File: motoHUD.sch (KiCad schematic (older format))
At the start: 54 parts

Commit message: update
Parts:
- added C? (x2): 10u, symbol Device:C_Small
- added C? (x2): 22u, symbol Device:C_Small
- added C? (x2): 2,2u, symbol Device:C_Small
- added D? (x3): 1N4148, Diode_THT:D_DO-35_SOD27_P7.62mm_Horizontal, symbol Diode:1N4148
- added J?: SIG_CONN, symbol Connector:Conn_01x03_Female
- added J?: Ignition 12V, symbol Connector:Conn_01x02_Female
- added J?: Constant 12V, symbol Connector:Conn_01x02_Female
- added R? (x3): 10k, symbol Device:R
- added R? (x3): 3k3, symbol Device:R
- added R?: 100k, symbol Device:R
- added R?: 22k, symbol Device:R
- added R?: 75R, symbol Device:R
- added TP?: RTCPWR, symbol Connector:TestPoint
- added U?: AZ1117-3.3, symbol Regulator_Linear:AZ1117-3.3
- added U?: AZ1117-5.0, symbol Regulator_Linear:AZ1117-5.0
- added U?: LM311, symbol Comparator:LM311
- added U?: PC817, Package_DIP:DIP-4_W7.62mm, symbol Isolator:PC817
- Q?: value Q_NMOS_DGS -> ????
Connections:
- net +3V3: now also C?.1, U?.2 (VO)
- net +5V: now also C?.1, C?.1, U?.2 (VO), U?.3 (VI)
- net GND: now also U?.23 (VSS), U?.35 (VSS), U?.47 (VSS), U?.8 (VSSA), C?.2, C?.2, C?.2, C?.2, C?.2, C?.2, J?.1 (Pin_1), J?.1 (Pin_1), R?.2, R?.2, R?.2, R?.2, U?.1 (GND), U?.1 (GND)
- net SIG_BLINK: now also R?.1, R?.2
- net SIG_HIBEAM: now also R?.1, R?.2
- net SIG_NEUTRAL: now also R?.1, R?.2
- net +BATT: now reaches U?.1 (VBAT)
- net +BATT: now also C?.1, R?.1, R?.2, TP?.1
- new net: J?.1 (Pin_1), R?.1
- new net: J?.2 (Pin_2), R?.1
- new net: J?.3 (Pin_3), R?.1
- new net: D?.1 (K), R?.1 (x2)
- new net: D?.2 (A), J?.2 (Pin_2) (x2)
- new net: C?.1, R?.2
- new net VCC: C?.1, D?.1 (K), U?.3 (VI)
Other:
- note added: "12-15V\nIgnition"
- note added: "2,9V for 12V in\n3,7V for 15V in\nMCU pins 5V tolerant"
- note added: "3.3V POWER RAIL"
- note added: "5V POWER RAIL"
- note added: "Backlight LED\nUf=3,2V\nIf=60mA"
- note added: "IGNITION INPUT"
- note added: "RC=10s"
- note added: "RTC POWER RAIL"
- note added: "RTC rated 1,8V-3,6V 20-24uA\n\n+BATT at\n2,37V at 12V 21uA load\n3,22V at 16V 26uA load\n134uA current consumption"
- note added: "SIGNAL INPUTS"
- note added: "VBAT 1.8-3,6V"
- note added: "White LED\nUf=3,2V"
- note added: "fc=964Hz"
- moved on the sheet: C?, D?, J?, M?, Q?, R?, TP?, U?, Y?

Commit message: RPM sensing
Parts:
- removed C?: 2,2u, symbol Device:C_Small
- removed D?: 1N4148, Diode_THT:D_DO-35_SOD27_P7.62mm_Horizontal, symbol Diode:1N4148
- removed J?: Conn_01x03_MountingPin, symbol Connector_Generic_MountingPin:Conn_01x03_MountingPin
- removed J?: SIG_CONN, symbol Connector:Conn_01x03_Female
- removed R?: 100k, symbol Device:R
- removed R?: 75R, symbol Device:R
- removed U?: PC817, Package_DIP:DIP-4_W7.62mm, symbol Isolator:PC817
- added C14, C15, C16: 0,1u, symbol Device:C_Small
- added C9: 2,2u, symbol Device:C_Small
- added F1: C1F-375, symbol Device:Fuse_Small
- added J6: SIG_RPM, symbol Connector:Conn_01x02_Female
- added J7: Conn_01x04_Female, symbol Connector:Conn_01x04_Female
- added J9: Conn_01x03_Male, symbol Connector:Conn_01x03_Male
- added R9: 10K, symbol Device:R
- gave numbers to parts that had none: 73
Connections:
- net +3V3: now also U3.8 (V+), C14.1, C15.1, C16.1, C9.1, R9.2
- net GND: now also U3.1 (GND), U3.3 (-), U3.4 (V-), C14.2, C15.2, C16.2, C9.2, J6.1 (Pin_1), J7.1 (Pin_1), J9.1 (Pin_1)
- net SIG_RPM: now also U3.7, R9.1
- net SWDCLK: now also J9.3 (Pin_3)
- net SWDIO: now also J9.2 (Pin_2)
- net at R16.1: now also J7.2 (Pin_2)
- net at R19.1: now also J7.3 (Pin_3)
- net at R21.1: now also J7.4 (Pin_4)
- net at J2.2 (Pin_2): now also F1.1; no longer D2.2 (A)
- net at U3.2 (+): now also J6.2 (Pin_2)
- net at U3.5 (BAL): now also U3.6 (STRB)
- new net: D2.2 (A), F1.2
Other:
- note added: "High level\n2,9V for 12V in\n3,7V for 15V in\nMCU pins 5V tolerant"
- note added: "RPM SENSING"
- note removed: "2,9V for 12V in\n3,7V for 15V in\nMCU pins 5V tolerant"
- note removed: "fc=964Hz"
- moved on the sheet: C1, C10, C11, C12, C13, C2, C5, C6, C7, D1, D2, D7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

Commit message: Updated PCB layout
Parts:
- removed C9: 2,2u, symbol Device:C_Small
- removed J1: Constant 12V, symbol Connector:Conn_01x02_Female
- removed J2: Ignition 12V, symbol Connector:Conn_01x02_Female
- removed J7: Conn_01x04_Female, symbol Connector:Conn_01x04_Female
- added D8: 1N4148, Diode_THT:D_DO-35_SOD27_P7.62mm_Horizontal, symbol Diode:1N4148
- added J1: POWER, Connector_JST:JST_XH_B03B-XH-A_1x03_P2.50mm_Vertical, symbol Connector:Conn_01x03_Female
- added J2: SIGNAL, Connector_JST:JST_XH_B03B-XH-A_1x03_P2.50mm_Vertical, symbol Connector:Conn_01x03_Female
- added R34, R35: 5,1k, Resistor_SMD:R_0805_2012Metric_Pad1.15x1.40mm_HandSolder, symbol Device:R
- added R36, R37: 100K, Resistor_SMD:R_0805_2012Metric_Pad1.15x1.40mm_HandSolder, symbol Device:R
- added R38: 10k, Resistor_SMD:R_0805_2012Metric_Pad1.15x1.40mm_HandSolder, symbol Device:R
- added R39: 20M, Resistor_SMD:R_0805_2012Metric_Pad1.15x1.40mm_HandSolder, symbol Device:R
- added TP6: PA0, TestPoint:TestPoint_Pad_D2.5mm, symbol Connector:TestPoint
- added TP7: PA1, TestPoint:TestPoint_Pad_D2.5mm, symbol Connector:TestPoint
- C1, C10, C11, C12, C13, C14, C15, C16, C2, C3, C4, C5, C6, C7: footprint (none) -> Capacitor_SMD:C_0805_2012Metric_Pad1.15x1.40mm_HandSolder
- C8: footprint (none) -> Capacitor_THT:CP_Radial_D8.0mm_P3.50mm
- D3, D4, D5, D6: footprint (none) -> LED_SMD:LED_1206_3216Metric
- D7: footprint (none) -> LED_SMD:LED_1206_3216Metric_Pad1.42x1.75mm_HandSolder
- F1: footprint (none) -> Fuse:Fuse_1206_3216Metric_Pad1.42x1.75mm_HandSolder
- J10: footprint (none) -> motoHUD:ILI9341 FFC
- J3, J4, J6: footprint (none) -> Connector_JST:JST_XH_B02B-XH-A_1x02_P2.50mm_Vertical
- J5: footprint (none) -> Connector_JST:JST_XH_B03B-XH-A_1x03_P2.50mm_Vertical
- J8: footprint (none) -> Connector_USB:USB_Mini-B_Lumberg_2486_01_Horizontal
- J9: footprint (none) -> Connector_PinHeader_2.54mm:PinHeader_1x03_P2.54mm_Vertical
- M1: footprint (none) -> motoHUD:X27-168
- Q1: value ????? -> 2N7002KQ-13; footprint (none) -> Package_TO_SOT_SMD:SOT-23
- Q2: value ???? -> 2N7002KQ-13; footprint (none) -> Package_TO_SOT_SMD:SOT-23
- R1, R10, R11, R12, R13, R14, R15, R16, R17, R18, R19, R2, R20, R21, R22, R23, R24, R25, R26, R27, R28, R29, R3, R30, R31, R32, R33, R4, R5, R6, R7, R8, R9: footprint (none) -> Resistor_SMD:R_0805_2012Metric_Pad1.15x1.40mm_HandSolder
- TP1, TP2, TP3, TP4, TP5: footprint (none) -> TestPoint:TestPoint_Pad_D2.5mm
- U1, U2: footprint (none) -> Package_TO_SOT_SMD:SOT-223
- U3: value LM311 -> LM2903DT; footprint (none) -> Package_SO:SOIC-8_3.9x4.9mm_P1.27mm
- Y1: footprint (none) -> Crystal:Crystal_SMD_HC49-SD_HandSoldering
- Y2: footprint (none) -> Crystal:Crystal_C26-LF_D2.1mm_L6.5mm_Horizontal
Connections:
- net +3V3: now also R36.2, R37.2
- net GND: now also D8.2 (A), J1.1 (Pin_1), R38.2; no longer U3.3 (-)
- net SIG_RPM: now also R39.2
- net at U4.10 (PA0): now also TP6.1
- net at U4.11 (PA1): now also TP7.1
- net at R16.1: now also J2.1 (Pin_1)
- net at R19.1: now also J2.2 (Pin_2)
- net at R21.1: now also J2.3 (Pin_3)
- net Ignition12V: now reaches F1.1
- net Ignition12V: now also J1.2 (Pin_2)
- net at J6.2 (Pin_2): now also R34.1; no longer U3.2 (+)
- net Constant12V: now reaches D1.2 (A)
- net Constant12V: now also J1.3 (Pin_3)
- new net: D8.1 (K), R34.2, R35.1
- new net: R35.2, R36.1, U3.3 (-)
- new net: R37.1, R38.1, R39.1, U3.2 (+)
- no-connect marks 4 -> 7
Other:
- note added: "2,8' TFT SPI display\nNo touch\nILI9341 driver\n\n1 GND\n2 RESET\n3 SCL\n4 D/C\n5 CS\n6 SDA\n7 SDO\n8 GND\n9 VCC\n10 LED Anode\n11-14 LED Cathode\n15-18 Touch"
- note added: "375mA fuse"
- note added: "7,6k R1 for best accuracy @90C\nVoltage is not linear to temp\nin this configuration"
- note added: "Circuit not tested on vehicle!"
- note added: "Configuration data storage\nSaving data like odometer, mileage etc.\nOnly RTC is powered when ignition is OFF"
- note added: "LM2903 datasheet\nTypical application fig.15\n\nTimer in MCU measures frequency\nof the signal, and calculates engine RPM"
- note added: "MPU programming and debugging"
- note added: "Motor load is so small\nit can be driven with MCU\npins directly (<20mA)\nCircuit tested, no voltage spikes."
- note added: "POWER CONNECTOR"
- note added: "RC filter for ADC noise canceling"
- note added: "RPM Zero-crossing detection"
- note added: "USB driver in STM32 set as CDC class(UART over USB)\nSerial communication for setting configuration parameters\nlike wheel circumference, RPM range etc.\n"
- note added: "Unipolar Hall sensor used\nwith magnets mounted\non wheel axle"
- note removed: "1 GND\n2 RESET\n3 SCL\n4 D/C\n5 CS\n6 SDA\n7 SDO\n8 GND\n9 VCC\n10 LED Anode\n11-14 LED Cathode\n15-18 Touch"
- note removed: "7,6k best accuracy for 90C"
- note removed: "RPM SENSING"
- moved on the sheet: D2, F1, J6, R9, TP5, U3

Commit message: schematic rev2
2nd revision schematic and updated BOM
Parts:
- removed C2: 10u, Capacitor_SMD:C_0805_2012Metric_Pad1.15x1.40mm_HandSolder, symbol Device:C_Small
- removed C3, C4: 2,2u, Capacitor_SMD:C_0805_2012Metric_Pad1.15x1.40mm_HandSolder, symbol Device:C_Small
- removed C7: 22u, Capacitor_SMD:C_0805_2012Metric_Pad1.15x1.40mm_HandSolder, symbol Device:C_Small
- removed R4, R5: 100K, Resistor_SMD:R_0805_2012Metric_Pad1.15x1.40mm_HandSolder, symbol Device:R
- removed U2: AZ1117-5.0, Package_TO_SOT_SMD:SOT-223, symbol Regulator_Linear:AZ1117-5.0
- removed U3: LM2903DT, Package_SO:SOIC-8_3.9x4.9mm_P1.27mm, symbol Comparator:LM311
- added C12, C14, C15: 10u 16v, Capacitor_SMD:C_0805_2012Metric_Pad1.15x1.40mm_HandSolder, symbol Device:C_Small
- added C13: 0,1u, Capacitor_SMD:C_0805_2012Metric_Pad1.15x1.40mm_HandSolder, symbol Device:C_Small
- added C16: 100u, Capacitor_THT:CP_Radial_D8.0mm_P3.50mm, symbol Device:CP
- added C22, C25: 22u, Capacitor_SMD:C_0805_2012Metric_Pad1.15x1.40mm_HandSolder, symbol Device:C_Small
- added D4: STPS1L40A, Diode_SMD:D_SMA_Handsoldering, symbol Diode:BAT48RL
- added D5: 1N4148W-7-F, Diode_SMD:D_SOD-123, symbol Diode:1N4148
- added L1: DLG-0403-220, Inductor_SMD:L_2816_7142Metric_Pad3.20x4.45mm_HandSolder, symbol Device:L
- added R13: 51,1k, Resistor_SMD:R_0805_2012Metric_Pad1.15x1.40mm_HandSolder, symbol Device:R
- added R14: 1,5k, Resistor_SMD:R_0805_2012Metric_Pad1.15x1.40mm_HandSolder, symbol Device:R
- added R15: 10k, Resistor_SMD:R_0805_2012Metric_Pad1.15x1.40mm_HandSolder, symbol Device:R
- added R16, R17, R32, R62: 0R, Resistor_SMD:R_0805_2012Metric_Pad1.15x1.40mm_HandSolder, symbol Device:R
- added R26: 2,2k, Resistor_SMD:R_0805_2012Metric_Pad1.15x1.40mm_HandSolder, symbol Device:R
- added SW1: TACTM-613N-F, Button_Switch_SMD:SW_SPST_EVQQ2, symbol Switch:SW_Push
- added TP10: TEMP1, TestPoint:TestPoint_THTPad_D2.5mm_Drill1.2mm, symbol Connector:TestPoint
- added TP11: TEMP2, TestPoint:TestPoint_THTPad_D2.5mm_Drill1.2mm, symbol Connector:TestPoint
- added TP12: RPMA, TestPoint:TestPoint_THTPad_D2.5mm_Drill1.2mm, symbol Connector:TestPoint
- added TP13: BOOST, TestPoint:TestPoint_THTPad_D2.5mm_Drill1.2mm, symbol Connector:TestPoint
- added TP14: BCKL_V, TestPoint:TestPoint_THTPad_D2.5mm_Drill1.2mm, symbol Connector:TestPoint
- added TP15: RPMC, TestPoint:TestPoint_THTPad_D2.5mm_Drill1.2mm, symbol Connector:TestPoint
- added TP16: RPMD, TestPoint:TestPoint_THTPad_D2.5mm_Drill1.2mm, symbol Connector:TestPoint
- added TP17: BLINK, TestPoint:TestPoint_THTPad_D2.5mm_Drill1.2mm, symbol Connector:TestPoint
- added TP18: BLINK12, TestPoint:TestPoint_THTPad_D2.5mm_Drill1.2mm, symbol Connector:TestPoint
- added TP19: HIBEAM, TestPoint:TestPoint_THTPad_D2.5mm_Drill1.2mm, symbol Connector:TestPoint
- added TP20: HIBEAM12, TestPoint:TestPoint_THTPad_D2.5mm_Drill1.2mm, symbol Connector:TestPoint
- added TP21: NTR, TestPoint:TestPoint_THTPad_D2.5mm_Drill1.2mm, symbol Connector:TestPoint
- added TP22: NTR12, TestPoint:TestPoint_THTPad_D2.5mm_Drill1.2mm, symbol Connector:TestPoint
- added TP23: CS2, TestPoint:TestPoint_THTPad_D2.5mm_Drill1.2mm, symbol Connector:TestPoint
- added TP24: SCK1, TestPoint:TestPoint_THTPad_D2.5mm_Drill1.2mm, symbol Connector:TestPoint
- added TP25: D/C, TestPoint:TestPoint_THTPad_D2.5mm_Drill1.2mm, symbol Connector:TestPoint
- added TP26: MOSI1, TestPoint:TestPoint_THTPad_D2.5mm_Drill1.2mm, symbol Connector:TestPoint
- added TP27: LCDCAP, TestPoint:TestPoint_THTPad_D2.5mm_Drill1.2mm, symbol Connector:TestPoint
- added TP28: CS1, TestPoint:TestPoint_THTPad_D2.5mm_Drill1.2mm, symbol Connector:TestPoint
- added TP29: MISO1, TestPoint:TestPoint_THTPad_D2.5mm_Drill1.2mm, symbol Connector:TestPoint
- added TP30: LCDV, TestPoint:TestPoint_THTPad_D2.5mm_Drill1.2mm, symbol Connector:TestPoint
- added TP31: SCK2, TestPoint:TestPoint_THTPad_D2.5mm_Drill1.2mm, symbol Connector:TestPoint
- added TP32: MOSI2, TestPoint:TestPoint_THTPad_D2.5mm_Drill1.2mm, symbol Connector:TestPoint
- added TP33: MISO2, TestPoint:TestPoint_THTPad_D2.5mm_Drill1.2mm, symbol Connector:TestPoint
- added TP4: V_IGN, TestPoint:TestPoint_THTPad_D2.5mm_Drill1.2mm, symbol Connector:TestPoint
- added TP6: 5V, TestPoint:TestPoint_THTPad_D2.5mm_Drill1.2mm, symbol Connector:TestPoint
- added U2, U3: LM2904DT, Package_SO:SO-8_5.3x6.2mm_P1.27mm, symbol Amplifier_Operational:LM2904
- added U5: MCP16301, Package_TO_SOT_SMD:SOT-23-6, symbol Regulator_Switching:MCP16301
- C17: renamed from C1; value 10u -> 10u 16v
- C21: renamed from C8; value 100u -> 22u; footprint Capacitor_THT:CP_Radial_D8.0mm_P3.50mm -> Capacitor_SMD:C_0805_2012Metric_Pad1.15x1.40mm_HandSolder
- D1, D2: value 1N4148 -> 1N4148W-7-F; footprint Diode_THT:D_DO-35_SOD27_P7.62mm_Horizontal -> Diode_SMD:D_SOD-123
- D3: renamed from D8; value 1N4148 -> 1N4148W-7-F; footprint Diode_THT:D_DO-35_SOD27_P7.62mm_Horizontal -> Diode_SMD:D_SOD-123
- F1: value C1F-375 -> ESKA FUSE 0805-FF PW 0A5; footprint Fuse:Fuse_1206_3216Metric_Pad1.42x1.75mm_HandSolder -> Capacitor_SMD:C_1206_3216Metric_Pad1.42x1.75mm_HandSolder
- J8: renamed from J9; value Conn_01x03_Male -> ICSP
- Q1, Q2: footprint Package_TO_SOT_SMD:SOT-23 -> motoHUD:SOT-23
- R21: renamed from R3; value 10K -> 10k
- R210: renamed from R39; value 20M -> 1M
- R211: renamed from R9; value 10K -> 10k
- R22: renamed from R1; value 7,6K -> 7,6k
- R23: renamed from R2; value 7,6K -> 7,6k
- R27: renamed from R36; value 100K -> 100k
- R28: renamed from R37; value 100K -> 100k
- R33: renamed from R10; value 4R -> 100R
- R34: renamed from R11; value 4R -> 100R
- R35: renamed from R12; value 4R -> 100R
- R36: renamed from R13; value 4R -> 100R
- R51: renamed from R23; value 10K -> 10k
- R52: renamed from R24; value 10K -> 10k
- R54: renamed from R14; value 100K -> 100k
- R55: renamed from R18; value 10K -> 10k
- R61: renamed from R25; value 1,5K -> 100k
- R63: renamed from R33; value 4R -> 39R
- R64: renamed from R32; value 4R -> 39R
- R65: renamed from R31; value 4R -> 39R
- R66: renamed from R30; value 4R -> 39R
- R73: renamed from R29; value 1,5K -> 1,5k
- R74: renamed from R28; value 510R -> 1,5k
- TP1: value THERM1 -> VEL; footprint TestPoint:TestPoint_Pad_D2.5mm -> TestPoint:TestPoint_THTPad_D2.5mm_Drill1.2mm
- TP2: value THERM2 -> 3v3; footprint TestPoint:TestPoint_Pad_D2.5mm -> TestPoint:TestPoint_THTPad_D2.5mm_Drill1.2mm
- TP3: value RTCPWR -> V_RTC; footprint TestPoint:TestPoint_Pad_D2.5mm -> TestPoint:TestPoint_THTPad_D2.5mm_Drill1.2mm
- TP5: renamed from TP4; footprint TestPoint:TestPoint_Pad_D2.5mm -> TestPoint:TestPoint_THTPad_D2.5mm_Drill1.2mm
- TP7: renamed from TP6; footprint TestPoint:TestPoint_Pad_D2.5mm -> TestPoint:TestPoint_THTPad_D2.5mm_Drill1.2mm
- TP8: renamed from TP7; footprint TestPoint:TestPoint_Pad_D2.5mm -> TestPoint:TestPoint_THTPad_D2.5mm_Drill1.2mm
- TP9: renamed from TP5; footprint TestPoint:TestPoint_Pad_D2.5mm -> TestPoint:TestPoint_THTPad_D2.5mm_Drill1.2mm
- Y1: value 8M -> HC49USM-FF3F18-8M
- Y2: value 32,768k -> LFXTAL009678; footprint Crystal:Crystal_C26-LF_D2.1mm_L6.5mm_Horizontal -> Crystal:Crystal_SMD_3215-2Pin_3.2x1.5mm
- renumbered C6 to C11, C5 to C18, C15 to C23, C16 to C24, C13 to C30, C12 to C31, C11 to C32, C10 to C33, C14 to C34, D7 to D10, D3 to D6, D4 to D7, D5 to D8, D6 to D9, J3 to J2, J4 to J3, J5 to J4, J6 to J5, J2 to J6, J8 to J7, J10 to J9, R6 to R11, R7 to R12, R34 to R24, R35 to R25, R38 to R29, R8 to R31, R16 to R41, R17 to R42, R19 to R43, R20 to R44, R21 to R45, R22 to R46, R15 to R53, R27 to R71, R26 to R72, U4 to U1, U1 to U4, U5 to U6
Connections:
- net +3V3: now also TP2.1, C22.1, R16.1, U2.8 (V+), U3.8 (V+); no longer C18.1, J9.10 (Pin_10), R33.1, R34.1, R35.1, R36.1, U4.2 (VO)
- net +5V: now also J9.10 (Pin_10), R33.1, R34.1, R35.1, R36.1, R17.1, TP6.1
- net EEPROM_CS: now also TP23.1
- net EEPROM_MISO: now also TP33.1
- net EEPROM_MOSI: now also TP32.1
- net EEPROM_SCK: now also TP31.1
- net GND: now also D2.2 (A), C12.2, C14.2, C15.2, C16.2, C22.2, C25.2, D4.2 (A), R15.2, R26.1, SW1.2, U2.4 (V-), U3.4 (V-), U5.2 (GND)
- net LCD_CS: now also TP28.1
- net LCD_DC: now also TP25.1
- net LCD_MISO: now also TP29.1
- net LCD_MOSI: now also TP26.1
- net LCD_SCK: now also TP24.1
- net SIG_BLINK: now also TP18.1
- net SIG_HIBEAM: now also TP20.1
- net SIG_NEUTRAL: now also TP22.1
- net SIG_RPM: now also TP16.1, U3.1
- net SIG_TEMP1: now also U2.1, U2.2 (-); no longer TP1.1
- net SIG_TEMP2: now also U2.6 (-), U2.7; no longer TP2.1
- net SIG_VEL: now also TP1.1
- net VCC: now also F1.2, C12.1, C16.1, TP4.1, U5.4 (EN), U5.5 (Vin)
- net USERIN: now reaches TP8.1, U1.11 (PA1)
- net USERIN: now also SW1.1
- net at J2.1 (Pin_1), R22.1: now also TP10.1, U2.3 (+)
- net at J3.1 (Pin_1), R23.1: now also TP11.1, U2.5 (+)
- net at D6.1 (K), D7.1 (K), D9.1 (K)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: now also R32.2, TP14.1; no longer D8.1 (K)
- net at R63.2, R64.2, R65.2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: now also R62.1; no longer Q2.1 (D)
- net at Q2.2 (G), R61.1: now also C25.1, TP27.1
- net at J6.1 (Pin_1), R41.1: now also TP17.1
- net at J6.2 (Pin_2), R43.1: now also TP19.1
- net at J6.3 (Pin_3), R45.1: now also TP21.1
- net at R25.2, R27.1: now also R26.2, TP12.1, U3.2 (-)
- net at R210.1, R28.1, R29.1: now also TP15.1, U3.3 (+)
- new net: D8.1 (K), R32.1
- new net: Q2.1 (D), R62.2, TP30.1
- new net: C18.1, R16.2, U4.2 (VO)
- new net: C13.1, D5.1 (K), TP13.1, U5.1 (BOOST)
- new net: R14.2, R15.1, U5.3 (Vfb)
- new net: C13.2, D4.1 (K), L1.1, U5.6 (SW)
- new net: C14.1, C15.1, D5.2 (A), L1.2, R13.1, R17.2
- new net: R13.2, R14.1
- no-connect marks 7 -> 10
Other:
- note added: "32,768k"
- note added: "500mA fuse\nReverse pol. diode protection"
- note added: "MCU programming and debugging"
- note added: "Timer in MCU measures frequency\nof the signal, and calculates engine RPM"
- note added: "USER INPUT"
- note removed: "12-15V\nIgnition"
- note removed: "375mA fuse"
- note removed: "LM2903 datasheet\nTypical application fig.15\n\nTimer in MCU measures frequency\nof the signal, and calculates engine RPM"
- note removed: "MPU programming and debugging"
- note removed: "RC filter for ADC noise canceling"
- note removed: "RC=10s"
- moved on the sheet: C11, C23, C24, C30, C31, C32, C33, C34, D1, D10, D2, D3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

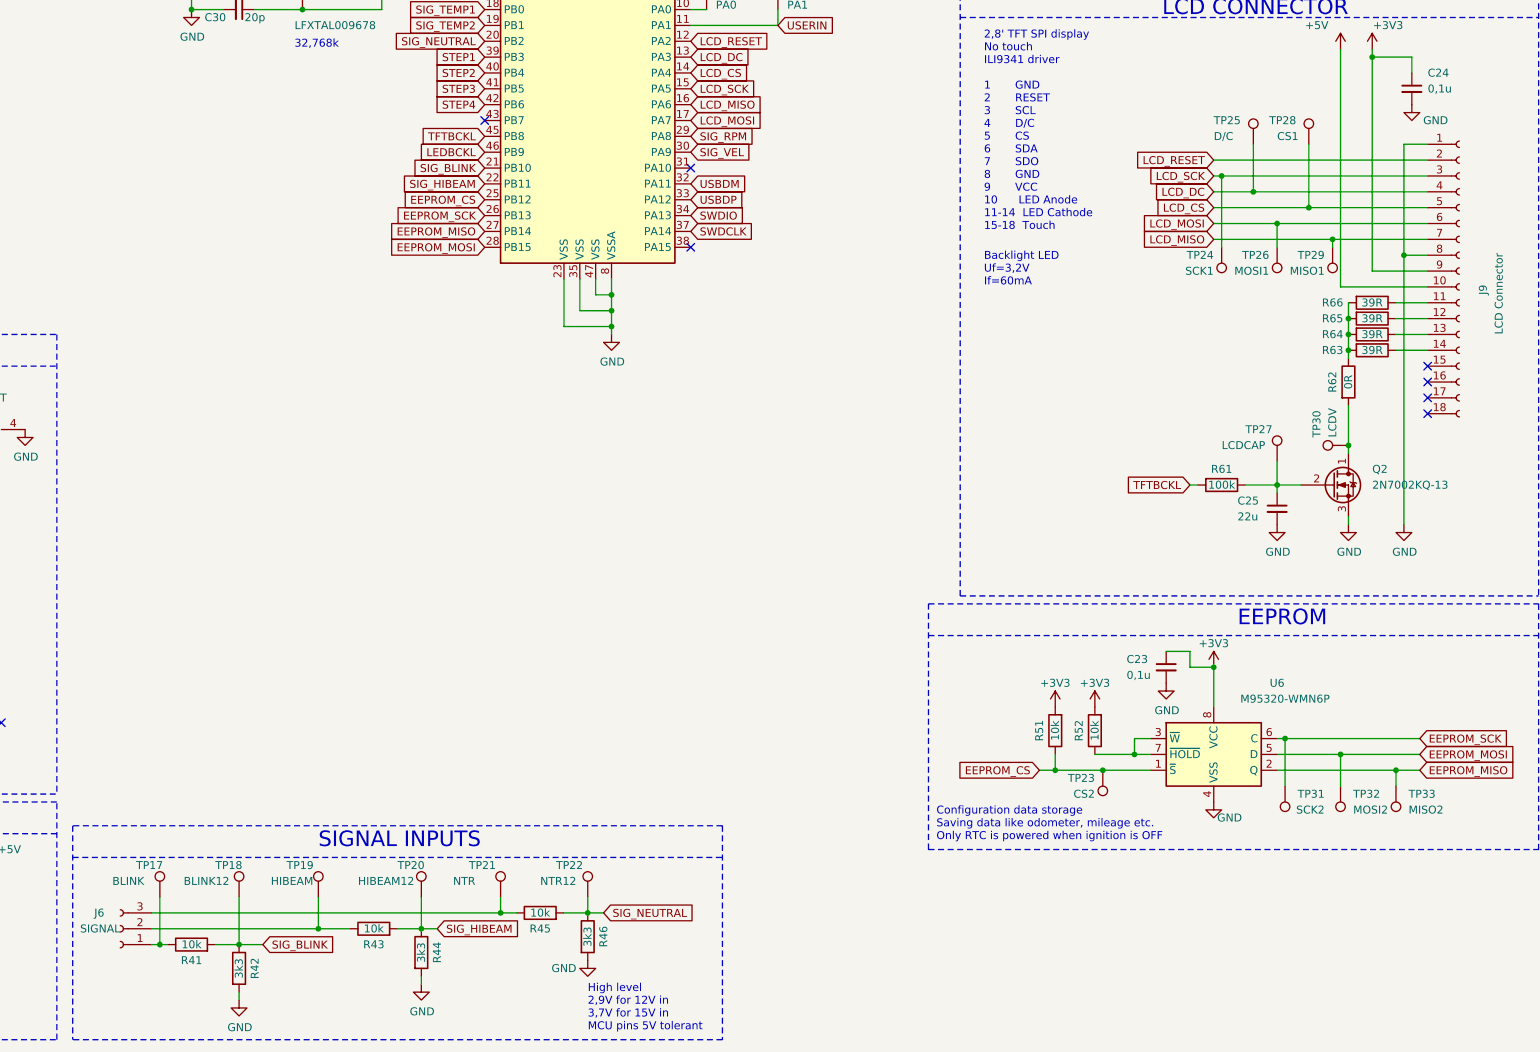
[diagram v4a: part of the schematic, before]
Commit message: rev2 layout and footprints updated
routing TODO
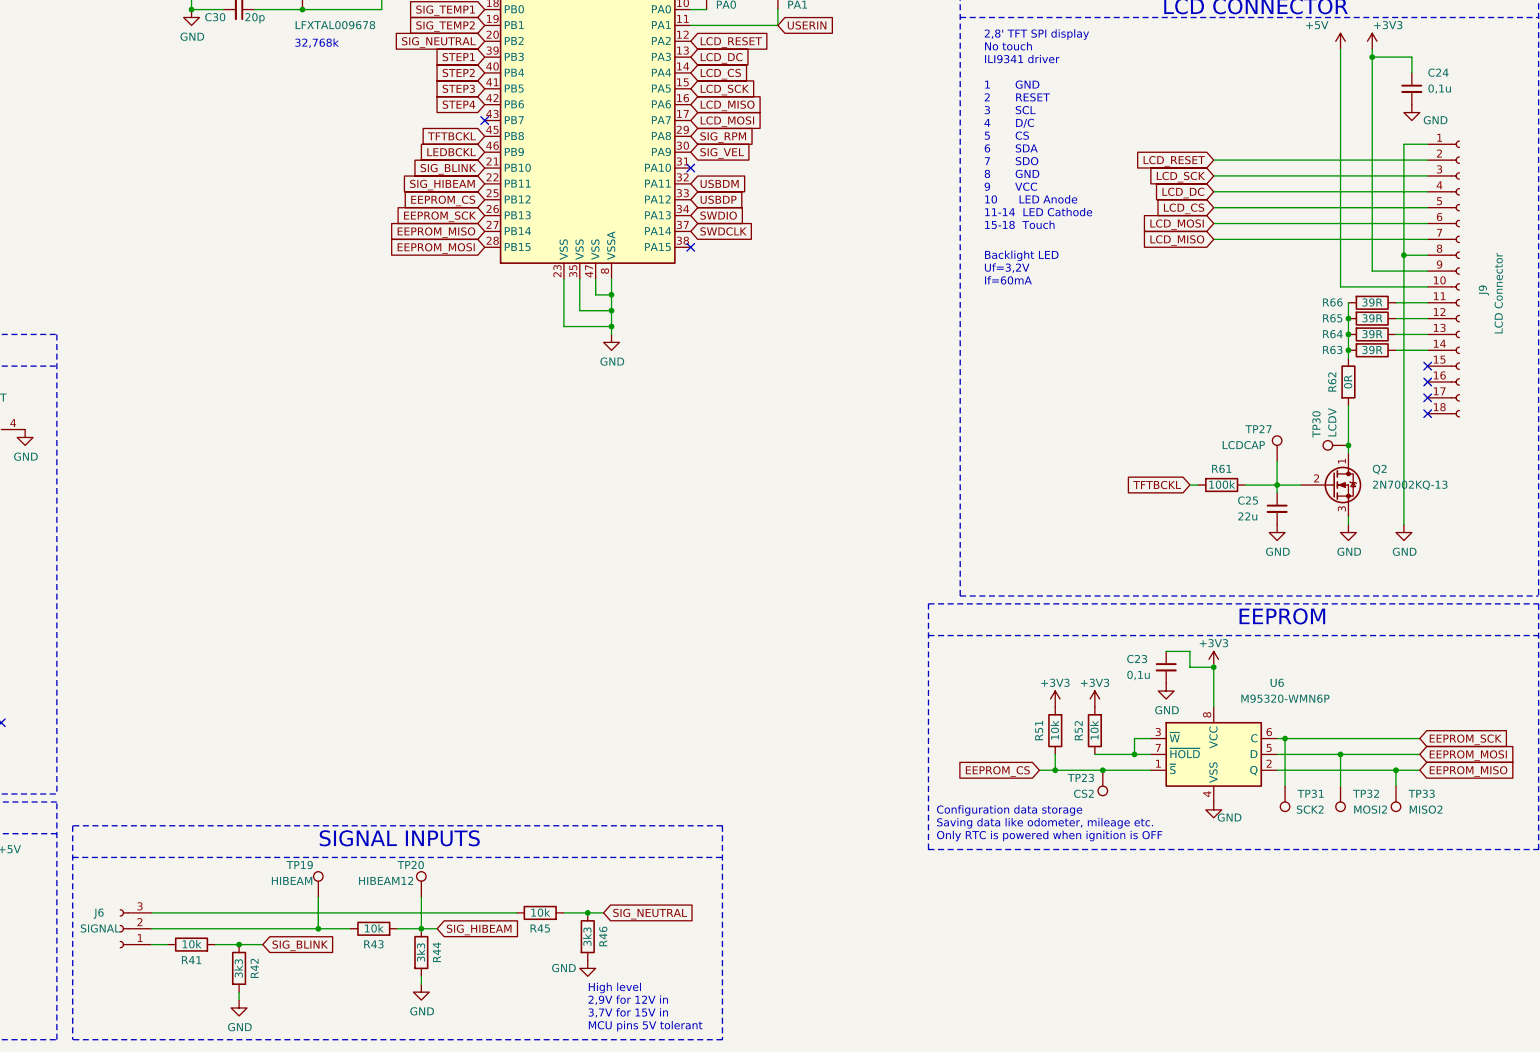
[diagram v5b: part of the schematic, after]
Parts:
- removed TP17: BLINK, TestPoint:TestPoint_THTPad_D2.5mm_Drill1.2mm, symbol Connector:TestPoint
- removed TP18: BLINK12, TestPoint:TestPoint_THTPad_D2.5mm_Drill1.2mm, symbol Connector:TestPoint
- removed TP21: NTR, TestPoint:TestPoint_THTPad_D2.5mm_Drill1.2mm, symbol Connector:TestPoint
- removed TP22: NTR12, TestPoint:TestPoint_THTPad_D2.5mm_Drill1.2mm, symbol Connector:TestPoint
- removed TP24: SCK1, TestPoint:TestPoint_THTPad_D2.5mm_Drill1.2mm, symbol Connector:TestPoint
- removed TP25: D/C, TestPoint:TestPoint_THTPad_D2.5mm_Drill1.2mm, symbol Connector:TestPoint
- removed TP26: MOSI1, TestPoint:TestPoint_THTPad_D2.5mm_Drill1.2mm, symbol Connector:TestPoint
- removed TP28: CS1, TestPoint:TestPoint_THTPad_D2.5mm_Drill1.2mm, symbol Connector:TestPoint
- removed TP29: MISO1, TestPoint:TestPoint_THTPad_D2.5mm_Drill1.2mm, symbol Connector:TestPoint
- J9: footprint motoHUD:ILI9341 FFC -> motoHUD:ILI9341FFC
- L1: footprint Inductor_SMD:L_2816_7142Metric_Pad3.20x4.45mm_HandSolder -> motoHUD:DLG-0403-220
- SW1: footprint Button_Switch_SMD:SW_SPST_EVQQ2 -> motoHUD:TACTM-613N-F
- TP1, TP10, TP11, TP12, TP13, TP14, TP15, TP16, TP19, TP2, TP20, TP23, TP27, TP3, TP30, TP31, TP32, TP33, TP4, TP5, TP6, TP7, TP8, TP9: footprint TestPoint:TestPoint_THTPad_D2.5mm_Drill1.2mm -> motoHUD:TestPoint_THTPad_D2.5mm_Drill1.2mm
- U4: footprint Package_TO_SOT_SMD:SOT-223 -> motoHUD:SOT-223
